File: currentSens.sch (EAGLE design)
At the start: 3 parts, among them U1 ATMEGA328P_VQFNVQFN

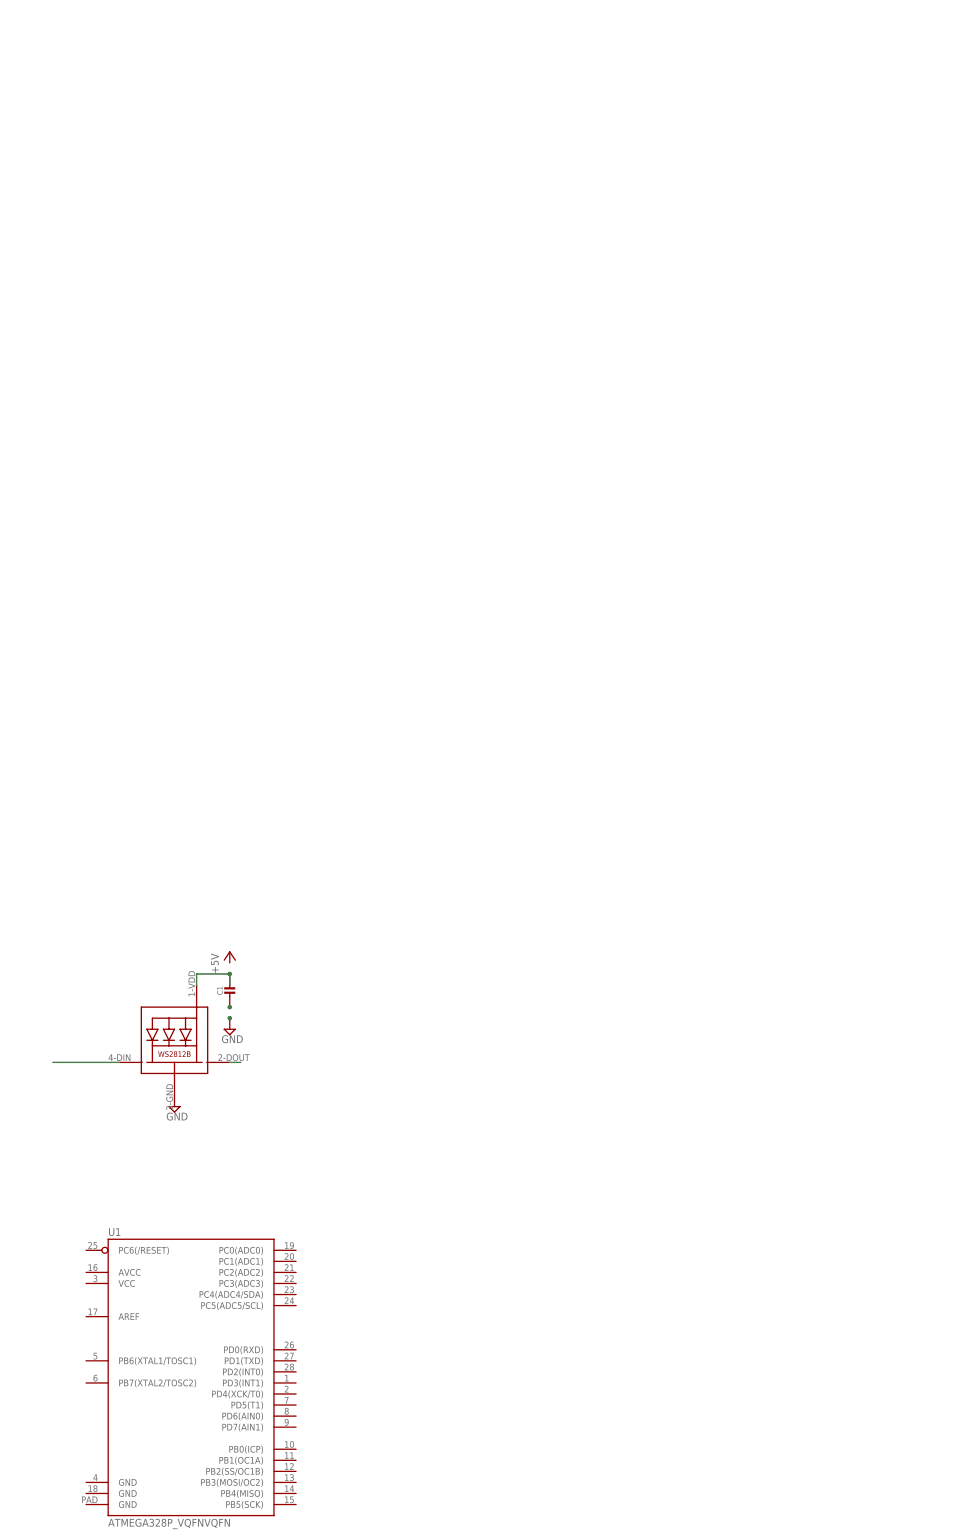
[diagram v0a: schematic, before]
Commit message: Added more neopixels
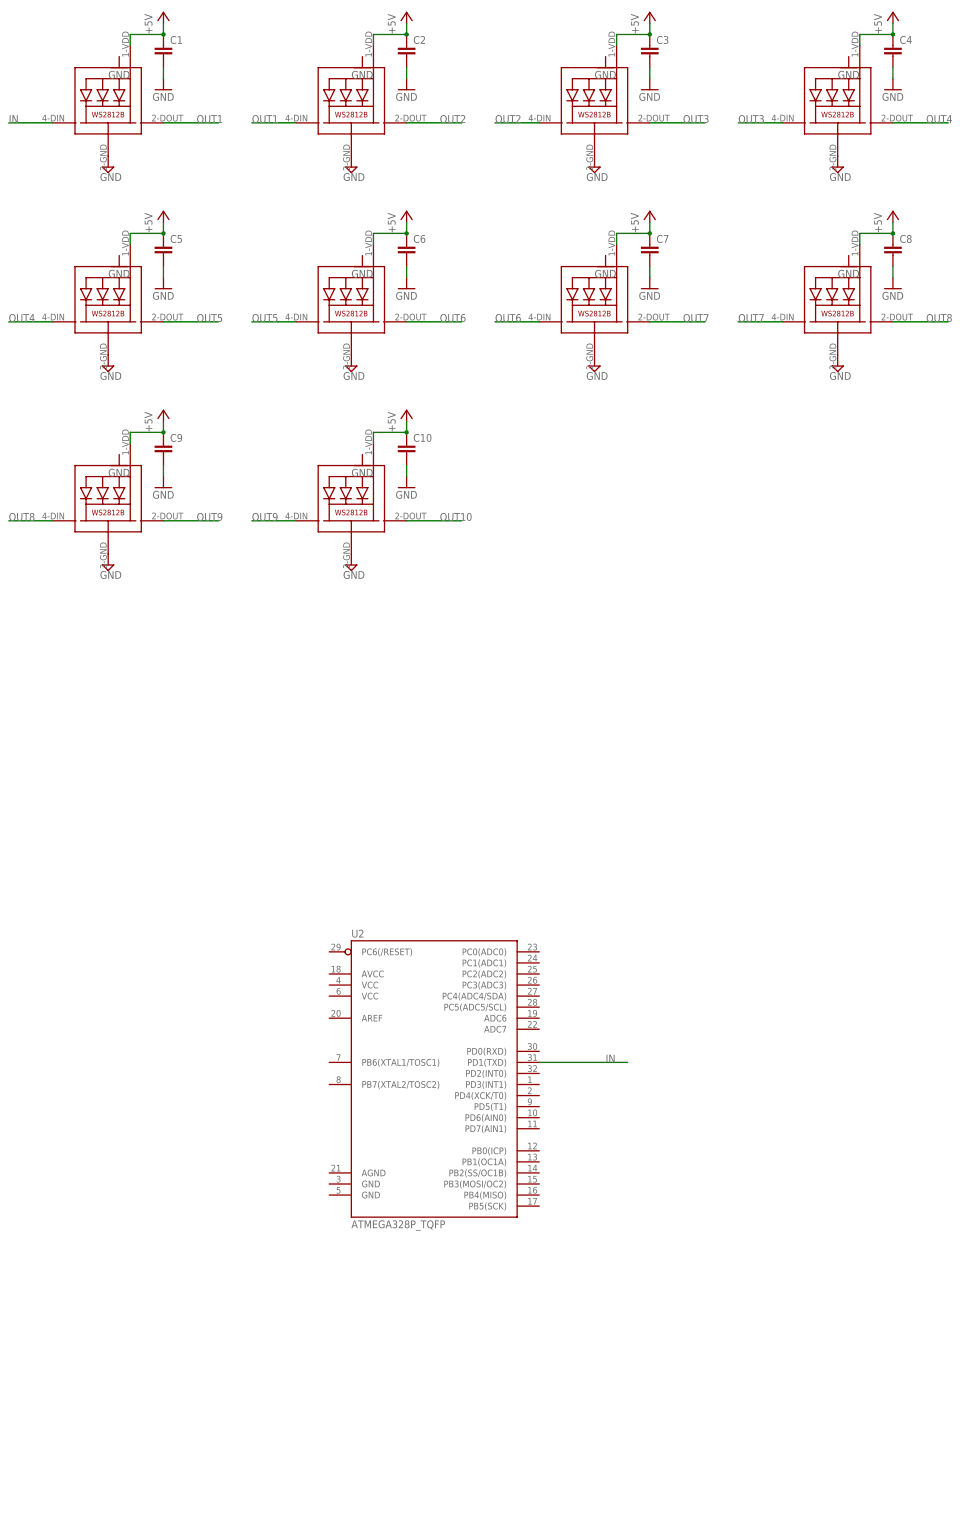
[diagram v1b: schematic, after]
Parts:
- removed U1: ATMEGA328P_VQFNVQFN, sensorsAndLights:ATMEGA328P_VQFNVQFN
- added C10, C2, C3, C4, C5, C6, C7, C8, C9: (no value), rcl:C-EUC0603
- added LED10, LED2, LED3, LED4, LED5, LED6, LED7, LED8, LED9: WS2812B5050, microbuilder:WS2812B5050
- added U2: ATMEGA328P_TQFP, SparkFun-IC-Microcontroller:ATMEGA328P_TQFP
- C1: device microbuilder:CAP_CERAMIC0805-NOOUTLINE -> rcl:C-EUC0603
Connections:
- removed net N$1: LED1.DI
- removed net N$59: LED1.DO
- removed net VDD: C1.1, LED1.VDD
- new net +5V: C1.1, C10.1, C2.1, C3.1, C4.1, C5.1, C6.1, C7.1, C8.1, C9.1, LED1.VDD, LED10.VDD, LED2.VDD, LED3.VDD, LED4.VDD, LED5.VDD, LED6.VDD, LED7.VDD, LED8.VDD, LED9.VDD
- new net IN: LED1.DI, U2.PD1(TXD)
- new net OUT1: LED1.DO, LED2.DI
- new net OUT10: LED10.DO
- new net OUT2: LED2.DO, LED3.DI
- new net OUT3: LED3.DO, LED4.DI
- new net OUT4: LED4.DO, LED5.DI
- new net OUT5: LED5.DO, LED6.DI
- new net OUT6: LED6.DO, LED7.DI
- new net OUT7: LED7.DO, LED8.DI
- new net OUT8: LED8.DO, LED9.DI
- new net OUT9: LED10.DI, LED9.DO
- net GND: now also C10.2, C2.2, C3.2, C4.2, C5.2, C6.2, C7.2, C8.2, C9.2, LED10.GND, LED2.GND, LED3.GND, LED4.GND, LED5.GND, LED6.GND, LED7.GND, LED8.GND, LED9.GND
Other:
- moved on the sheet: C1

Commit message: Finshed up microcontroller circuit
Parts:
- added BOOT: SWITCH, DiscreteComponents:SWITCH
- added C11, C12, C13, C14, C15, C16, C17: (no value), rcl:C-EUC0603
- added J1: AVR_SPI_PROG_3X2NS, SparkFun-Connectors:AVR_SPI_PROG_3X2NS
- added R1: (no value), SparkFun-Resistors:RESISTOR0603
- added Y2: (no value), SparkFun-Clocks:CRYSTALPTH-HC49US
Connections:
- new net MISO: J1.1, U2.PB4(MISO)
- new net MOSI: J1.4, U2.PB3(MOSI/OC2)
- new net N$1: C16.1, U2.PB6(XTAL1/TOSC1), Y2.2
- new net N$2: C17.1, U2.PB7(XTAL2/TOSC2), Y2.1
- new net RESET: BOOT.P$2, C11.2, J1.5, R1.1, U2.PC6(/RESET)
- new net SCK: J1.3, U2.PB5(SCK)
- net +5V: now also C12.1, C13.1, C14.1, C15.1, J1.2, R1.2, U2.AREF, U2.AVCC, U2.VCC@4, U2.VCC@6
- net GND: now also BOOT.P$1, C11.1, C12.2, C13.2, C14.2, C15.2, C16.2, C17.2, J1.6, U2.AGND, U2.GND@3, U2.GND@5
